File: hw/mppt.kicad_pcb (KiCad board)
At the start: 4 copper layers, 100.1 x 55.1 mm, 357 parts, among them J201 1935776, J301 1935776, J302 1935776, Q301 SW_L, Q302 SW_H, SW201 SW_Push, U201 MCU_Nucleo_L432KC, U401 INA210, U402 INA210, U403 OPA990, U404 OPA990, U501 LMG1210RVRT

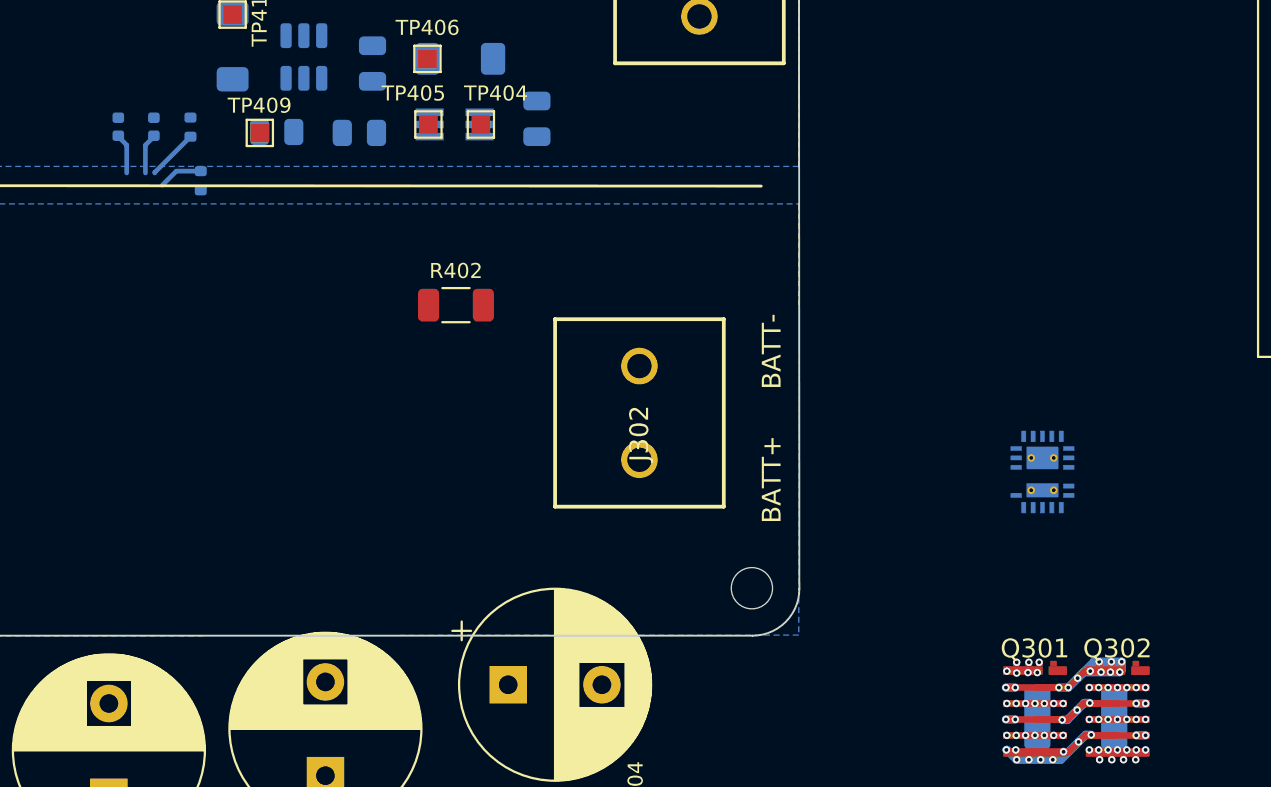
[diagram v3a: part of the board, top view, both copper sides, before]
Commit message: made gate driver loop v1
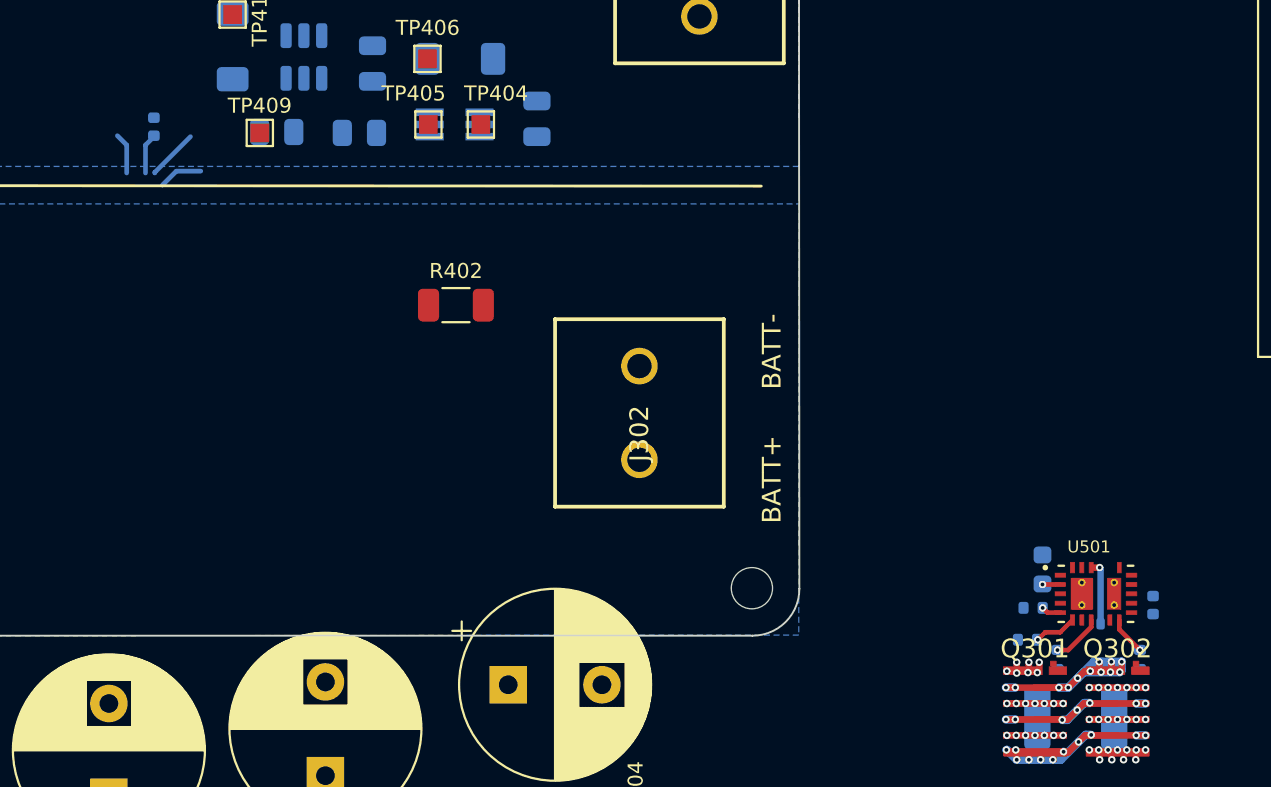
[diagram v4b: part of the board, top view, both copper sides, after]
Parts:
- added C503: 10uF, Capacitor_SMD:C_0402_1005Metric, B.Cu at (208.9, 113.4)
- added D1: Dboot, Diode_SMD:D_SOD-323, B.Cu at (206.1, 115.5)
- added R503: R_LO, Resistor_SMD:R_0402_1005Metric, B.Cu at (203.8, 116.3)
- added R504: R_HO, Resistor_SMD:R_0402_1005Metric, B.Cu at (208.2, 116.3)
- C502: footprint Capacitor_SMD:C_0402_1005Metric -> Capacitor_SMD:C_0603_1608Metric
- U501: moved to F.Cu
- moved C502 54.7 mm to (203.0, 111.5)
- moved R502 51.8 mm to (202.5, 113.5), turned to 180 degrees
- moved R501 50.4 mm to (202.2, 115.2), turned to 180 degrees
- moved U501 7.10 mm to (205.8, 112.8), turned to 0 degrees
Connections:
- net Net-(U501-DHL) renamed /gate_driver/DHL
- net Net-(U501-DLH) renamed /gate_driver/DLH
- net Net-(U501-HS-Pad13) renamed /gate_driver/HS
- L301 pad 2: /converter/V_SW -> V_SW
- Q301 pad 2: /converter/V_SW -> V_SW
- Q302 pad 3: /converter/V_SW -> V_SW
- U501 pad 10: /converter/SW2 -> /gate_driver/HO
- U501 pad 12: unconnected-(U501-HB-Pad12) -> V_SW
- U501 pad 17: unconnected-(U501-BST-Pad17) -> /gate_driver/BST
- U501 pad 8: /converter/SW1 -> /gate_driver/LO
- V1 pad 1: /converter/V_SW -> V_SW
- V10 pad 1: /converter/V_SW -> V_SW
- V11 pad 1: /converter/V_SW -> V_SW
- V12 pad 1: /converter/V_SW -> V_SW
- V13 pad 1: /converter/V_SW -> V_SW
- V14 pad 1: /converter/V_SW -> V_SW
- V15 pad 1: /converter/V_SW -> V_SW
- V16 pad 1: /converter/V_SW -> V_SW
- V17 pad 1: /converter/V_SW -> V_SW
- V18 pad 1: /converter/V_SW -> V_SW
- V19 pad 1: /converter/V_SW -> V_SW
- V2 pad 1: /converter/V_SW -> V_SW
- V20 pad 1: /converter/V_SW -> V_SW
- V21 pad 1: /converter/V_SW -> V_SW
- V22 pad 1: /converter/V_SW -> V_SW
- V23 pad 1: /converter/V_SW -> V_SW
- V24 pad 1: /converter/V_SW -> V_SW
- V25 pad 1: /converter/V_SW -> V_SW
- V26 pad 1: /converter/V_SW -> V_SW
- V27 pad 1: /converter/V_SW -> V_SW
- V28 pad 1: /converter/V_SW -> V_SW
- V29 pad 1: /converter/V_SW -> V_SW
- V3 pad 1: /converter/V_SW -> V_SW
- V30 pad 1: /converter/V_SW -> V_SW
- V31 pad 1: /converter/V_SW -> V_SW
- V32 pad 1: /converter/V_SW -> V_SW
- V33 pad 1: /converter/V_SW -> V_SW
- V34 pad 1: /converter/V_SW -> V_SW
- V35 pad 1: /converter/V_SW -> V_SW
- V36 pad 1: /converter/V_SW -> V_SW
- V37 pad 1: /converter/V_SW -> V_SW
- V38 pad 1: /converter/V_SW -> V_SW
- V39 pad 1: /converter/V_SW -> V_SW
- V4 pad 1: /converter/V_SW -> V_SW
- V40 pad 1: /converter/V_SW -> V_SW
- V41 pad 1: /converter/V_SW -> V_SW
- V42 pad 1: /converter/V_SW -> V_SW
- V43 pad 1: /converter/V_SW -> V_SW
- V44 pad 1: /converter/V_SW -> V_SW
- V45 pad 1: /converter/V_SW -> V_SW
- V46 pad 1: /converter/V_SW -> V_SW
- V47 pad 1: /converter/V_SW -> V_SW
- V48 pad 1: /converter/V_SW -> V_SW
- V49 pad 1: /converter/V_SW -> V_SW
- V5 pad 1: /converter/V_SW -> V_SW
- V50 pad 1: /converter/V_SW -> V_SW
- V51 pad 1: /converter/V_SW -> V_SW
- V52 pad 1: /converter/V_SW -> V_SW
- V53 pad 1: /converter/V_SW -> V_SW
- V54 pad 1: /converter/V_SW -> V_SW
- V55 pad 1: /converter/V_SW -> V_SW
- V56 pad 1: /converter/V_SW -> V_SW
- V57 pad 1: /converter/V_SW -> V_SW
- V58 pad 1: /converter/V_SW -> V_SW
- V59 pad 1: /converter/V_SW -> V_SW
- V6 pad 1: /converter/V_SW -> V_SW
- V60 pad 1: /converter/V_SW -> V_SW
- V61 pad 1: /converter/V_SW -> V_SW
- V62 pad 1: /converter/V_SW -> V_SW
- V63 pad 1: /converter/V_SW -> V_SW
- V64 pad 1: /converter/V_SW -> V_SW
- V65 pad 1: /converter/V_SW -> V_SW
- V66 pad 1: /converter/V_SW -> V_SW
- V67 pad 1: /converter/V_SW -> V_SW
- V68 pad 1: /converter/V_SW -> V_SW
- V69 pad 1: /converter/V_SW -> V_SW
- V7 pad 1: /converter/V_SW -> V_SW
- V70 pad 1: /converter/V_SW -> V_SW
- V71 pad 1: /converter/V_SW -> V_SW
- V72 pad 1: /converter/V_SW -> V_SW
- V73 pad 1: /converter/V_SW -> V_SW
- V74 pad 1: /converter/V_SW -> V_SW
- V75 pad 1: /converter/V_SW -> V_SW
- V76 pad 1: /converter/V_SW -> V_SW
- V77 pad 1: /converter/V_SW -> V_SW
- V78 pad 1: /converter/V_SW -> V_SW
- V79 pad 1: /converter/V_SW -> V_SW
- V8 pad 1: /converter/V_SW -> V_SW
- V80 pad 1: /converter/V_SW -> V_SW
- V81 pad 1: /converter/V_SW -> V_SW
- V82 pad 1: /converter/V_SW -> V_SW
- V83 pad 1: /converter/V_SW -> V_SW
- V84 pad 1: /converter/V_SW -> V_SW
- V85 pad 1: /converter/V_SW -> V_SW
- V86 pad 1: /converter/V_SW -> V_SW
- V87 pad 1: /converter/V_SW -> V_SW
- V88 pad 1: /converter/V_SW -> V_SW
- V89 pad 1: /converter/V_SW -> V_SW
- V9 pad 1: /converter/V_SW -> V_SW
- V90 pad 1: /converter/V_SW -> V_SW
- V91 pad 1: /converter/V_SW -> V_SW
- V92 pad 1: /converter/V_SW -> V_SW
- V93 pad 1: /converter/V_SW -> V_SW
- V94 pad 1: /converter/V_SW -> V_SW
- V95 pad 1: /converter/V_SW -> V_SW
- V96 pad 1: /converter/V_SW -> V_SW
- V97 pad 1: /converter/V_SW -> V_SW
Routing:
- net V_SW: track 0.00 -> 96.6 mm, vias 0 -> 30
- net /converter/V_SW: track 96.6 -> 0.00 mm, vias 31 -> 0
- net /gate_driver/BST: track 0.00 -> 3.32 mm, vias 0 -> 1
- net /gate_driver/LO: track 0.00 -> 2.68 mm, vias 0 -> 1
- net /gate_driver/DLH: track 2.36 -> 4.64 mm, vias 0 -> 1
- net /gate_driver/HO: track 0.00 -> 2.06 mm, vias 0 -> 1
- net /gate_driver/DHL: track 2.72 -> 3.77 mm, vias 0 -> 1
- net +12V: track 2.19 -> 3.14 mm, vias 0 -> 1
- net (no net): vias 0 -> 1

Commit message: layout revision this one is cursed
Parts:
- removed REF** (x7): Via_0.4mmOD_0.2mmID, mppt:Via_0.4mmOD_0.2mmID
- removed V1, V10, V100, V101, V102, V103, V104, V105, V106, V107, V108, V109, V11, V110, V111, V112, V113, V114, V115, V116, V117, V118, V119, V12, V120, V121, V122, V123, V124, V125, V126, V127, V128, V129, V13, V130, V131, V132, V133, V134, V135, V136, V137, V138, V139, V14, V140, V141, V142, V143, V144, V145, V146, V147, V148, V149, V15, V150, V151, V152, V153, V154, V155, V156, V157, V158, V159, V16, V160, V161, V162, V163, V164, V165, V166, V167, V168, V169, V17, V170, V171, V172, V173, V174, V175, V176, V177, V178, V179, V18, V180, V181, V182, V183, V184, V185, V186, V187, V188, V189, V19, V190, V191, V192, V193, V194, V195, V196, V197, V198, V199, V2, V20, V200, V201, V202, V203, V204, V205, V206, V207, V208, V209, V21, V210, V211, V212, V213, V214, V215, V216, V217, V218, V219, V22, V220, V221, V222, V223, V224, V225, V226, V227, V228, V229, V23, V230, V231, V232, V233, V234, V235, V236, V237, V238, V239, V24, V240, V241, V242, V243, V244, V245, V246, V247, V248, V249, V25, V250, V251, V252, V253, V254, V255, V256, V257, V258, V259, V26, V260, V261, V262, V263, V264, V265, V266, V267, V268, V269, V27, V270, V271, V272, V273, V274, V275, V276, V277, V278, V279, V28, V280, V281, V282, V283, V284, V285, V286, V287, V288, V289, V29, V3, V30, V31, V32, V33, V34, V35, V36, V37, V38, V39, V4, V40, V41, V42, V43, V44, V45, V46, V47, V48, V49, V5, V50, V51, V52, V53, V54, V55, V56, V57, V58, V59, V6, V60, V61, V62, V63, V64, V65, V66, V67, V68, V69, V7, V70, V71, V72, V73, V74, V75, V76, V77, V78, V79, V8, V80, V81, V82, V83, V84, V85, V86, V87, V88, V89, V9, V90, V91, V92, V93, V94, V95, V96, V97, V98, V99: 0.4mmVia, mppt:Via_0.4mmOD_0.2mmID
- L301: value 1529uH -> 560; footprint Inductor_THT:L_CommonMode_Toroid_Vertical_L43.2mm_W22.9mm_Px17.78mm_Py30.48mm_Bourns_8100 -> mppt:B65812N1005D002
- R201, R202, R203: moved to B.Cu
- moved L301 104.9 mm to (121.2, 111.9)
- moved SW201 63.5 mm to (109.3, 74.2), turned to 180 degrees
- moved C1 56.7 mm to (152.3, 98.1)
- moved C503 56.7 mm to (156.4, 92.1)
- moved C502 56.7 mm to (150.5, 90.2)
- moved D1 56.7 mm to (153.6, 94.2)
- moved Q301 56.7 mm to (150.1, 97.6)
- moved Q302 56.7 mm to (154.5, 97.6)
- moved R501 56.7 mm to (149.7, 94.0)
- moved R502 56.7 mm to (150.0, 92.2)
- moved R503 56.7 mm to (151.3, 95.0)
- moved R504 56.7 mm to (155.7, 95.0)
- moved U501 56.7 mm to (153.3, 91.5)
- moved C302 23.6 mm to (162.5, 99.0)
- moved D202 14.1 mm to (113.4, 75.9), turned to 180 degrees
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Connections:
- net V_SW renamed /converter/V_SW
- D1 pad 2: /gate_driver/BST -> +5V
- U501 pad 17: /gate_driver/BST -> +5V
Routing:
- net +12V: track 3.14 -> 126.6 mm, vias 1 -> 10
- net /controller/Reset: track 0.00 -> 51.8 mm
- net /controller/ARR_CURRENT: track 0.00 -> 45.1 mm, vias 0 -> 2
- net /controller/BATT_CURRENT: track 0.00 -> 44.7 mm, vias 0 -> 8
- net /controller/ARR_VOLTAGE: track 0.00 -> 36.6 mm, vias 0 -> 2
- net /controller/BATT_VOLTAGE: track 0.00 -> 33.0 mm, vias 0 -> 4
- net GND: track 0.00 -> 26.7 mm, vias 21 -> 28
- net /controller/PWM_EN: track 0.00 -> 25.6 mm
- net /converter/V_ARR+: track 0.00 -> 23.6 mm, vias 0 -> 1
- net /controller/PWM: track 0.00 -> 23.2 mm, vias 0 -> 4
- net +5V: track 2.19 -> 21.7 mm, vias 0 -> 4
- net /controller/Heartbeat: track 0.00 -> 15.8 mm, vias 0 -> 1
- net /converter/V_ARR-: track 0.00 -> 12.5 mm, vias 0 -> 1
- net /controller/Tracking: track 0.00 -> 11.3 mm, vias 0 -> 1
- net /converter/V_BATT-: track 0.00 -> 9.94 mm, vias 0 -> 1
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- added copper zone on F.Cu, net /converter/V_ARR+
- added copper zone on F.Cu, net /converter/V_ARR-
- added copper zone on In1.Cu, net /converter/V_ARR-
- added copper zone on F.Cu, net /converter/V_BATT-
- added copper zone on In1.Cu, net /converter/V_BATT-
- added copper zone on F.Cu, net GND
- removed copper zone on B.Cu, net /converter/V_BATT+
- removed copper zone on In1.Cu, net /converter/V_BATT+
- removed copper zone on In2.Cu, net /converter/V_BATT+
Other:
- board size 100.1 x 55.1 mm -> 100.1 x 48.6 mm
- board text added: "INCOMPLETE"
- board text added: "LAYOUT WILL BE REVISED SIGNIFICANTLY"
- board text added: "PENDING"

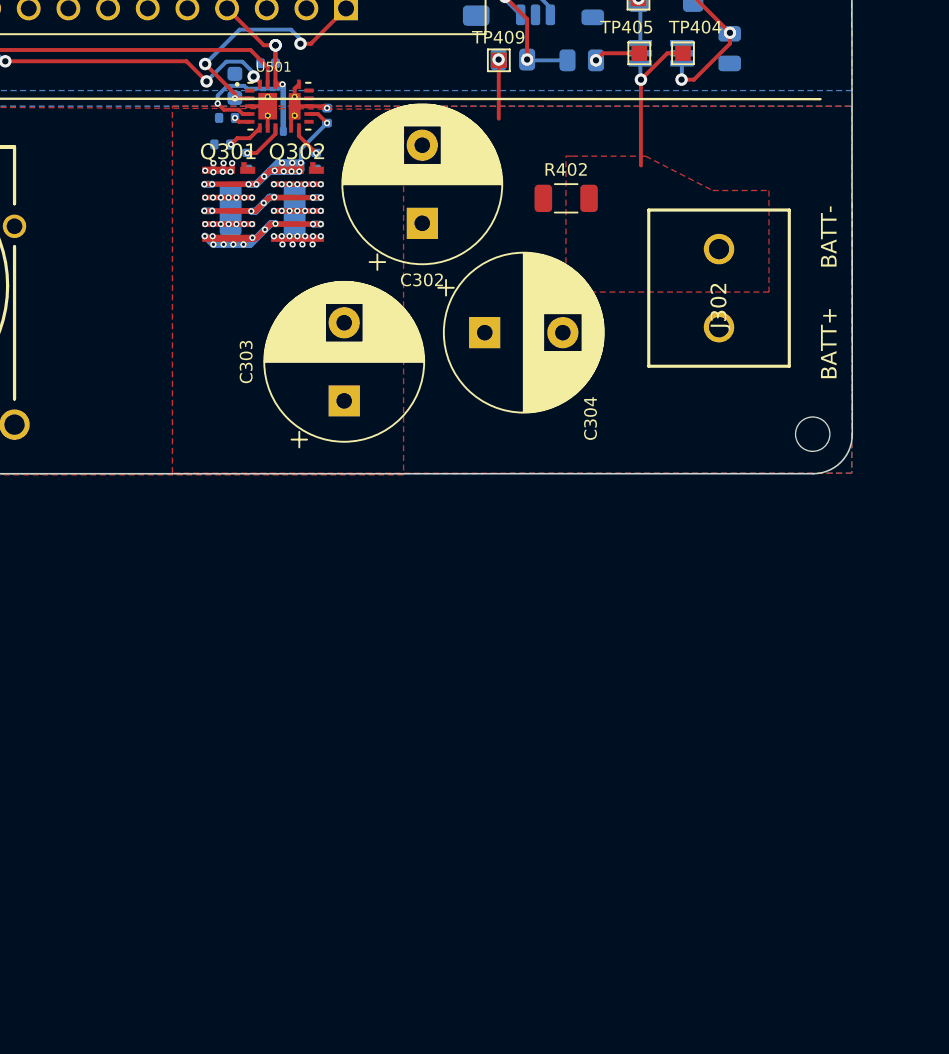
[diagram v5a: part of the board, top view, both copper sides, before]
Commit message: improved thermals of fets with internal vias, internal traces, and thermal jumpers
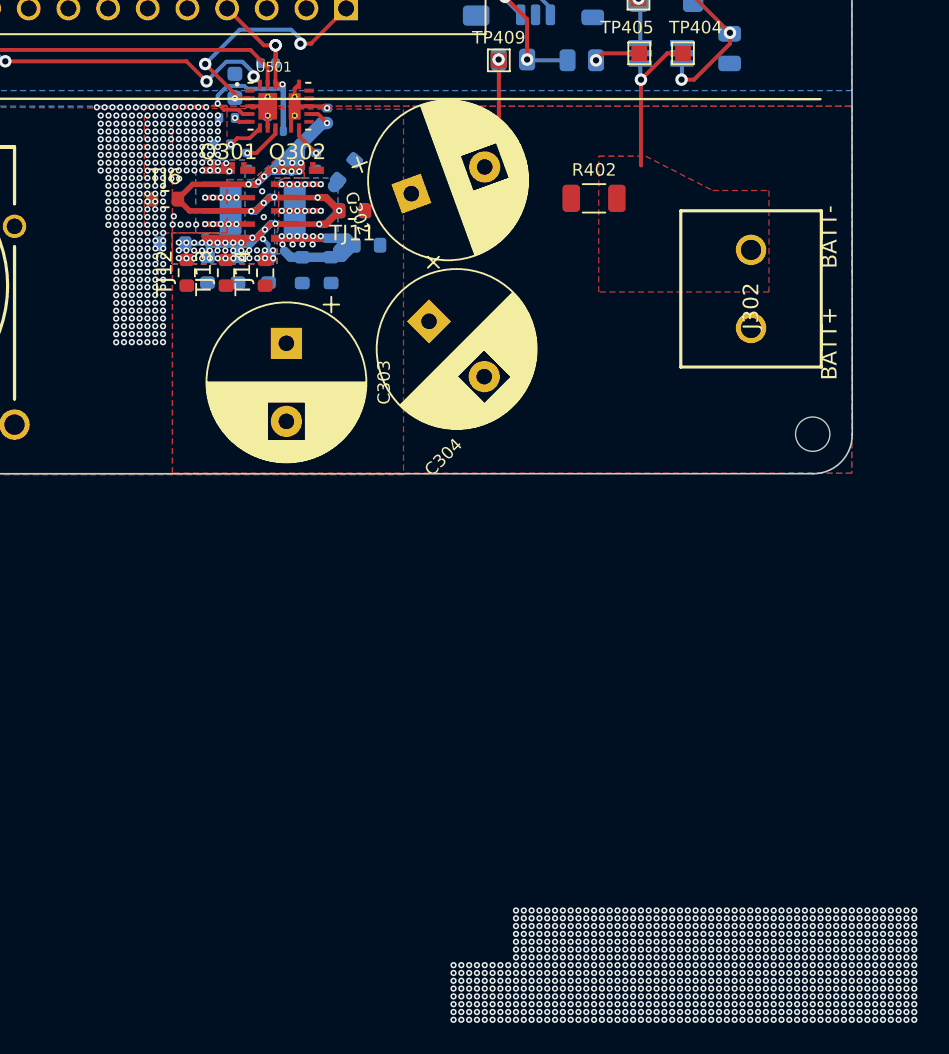
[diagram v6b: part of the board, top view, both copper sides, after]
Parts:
- added TJ1: Thermal Jumper, Resistor_SMD:R_0603_1608Metric, B.Cu at (148.8, 102.0)
- added TJ10: Thermal Jumper, Resistor_SMD:R_0603_1608Metric, B.Cu at (157.6, 95.6)
- added TJ11: Thermal Jumper, Resistor_SMD:R_0603_1608Metric, F.Cu at (158.0, 98.2)
- added TJ12: Thermal Jumper, Resistor_SMD:R_0603_1608Metric, F.Cu at (147.4, 102.2)
- added TJ13: Thermal Jumper, Resistor_SMD:R_0603_1608Metric, F.Cu at (149.9, 102.2)
- added TJ14: Thermal Jumper, Resistor_SMD:R_0603_1608Metric, F.Cu at (152.4, 102.2)
- added TJ2: Thermal Jumper, Resistor_SMD:R_0603_1608Metric, B.Cu at (150.7, 102.0)
- added TJ3: Thermal Jumper, Resistor_SMD:R_0603_1608Metric, B.Cu at (152.7, 102.0)
- added TJ4: Thermal Jumper, Resistor_SMD:R_0603_1608Metric, B.Cu at (146.5, 100.3)
- added TJ5: Thermal Jumper, Resistor_SMD:R_0603_1608Metric, B.Cu at (158.0, 98.2)
- added TJ6: Thermal Jumper, Resistor_SMD:R_0603_1608Metric, F.Cu at (146.0, 97.5)
- added TJ7: Thermal Jumper, Resistor_SMD:R_0603_1608Metric, B.Cu at (159.0, 100.4)
- added TJ8: Thermal Jumper, Resistor_SMD:R_0603_1608Metric, B.Cu at (156.7, 102.0)
- added TJ9: Thermal Jumper, Resistor_SMD:R_0603_1608Metric, B.Cu at (154.8, 102.0)
- moved C303 5.22 mm to (153.8, 106.7), turned to -90 degrees
- moved C304 3.64 mm to (162.9, 105.3), turned to -45 degrees
- moved J302 2.05 mm to (183.6, 105.7)
- moved C302 2.02 mm to (161.8, 97.1), turned to 20 degrees
- moved R402 1.79 mm to (173.5, 97.4)
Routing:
- net /converter/V_SW: track 101.2 -> 110.4 mm, vias 31 -> 58
- net /converter/V_BATT+: track 3.83 -> 12.6 mm, vias 26 -> 23
- net GND: track 26.7 -> 31.8 mm, vias 28 -> 330
- net (no net): vias 0 -> 844
- added copper zone on B.Cu, net /converter/V_BATT+
- added copper zone on In1.Cu, net /converter/V_BATT+
- added copper zone on In2.Cu, net /converter/V_BATT+
- added copper zone on B.Cu, net /converter/V_SW
- added copper zone on F.Cu, net /converter/V_SW
- added copper zone on In1.Cu, net /converter/V_SW
- added copper zone on In2.Cu, net /converter/V_SW
- added copper zone on In1.Cu, net GND
- added copper zone on In2.Cu, net GND
